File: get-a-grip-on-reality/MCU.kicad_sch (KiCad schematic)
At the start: 20 parts, among them J2 USB_OTG, U3 ESP32-S3-WROOM-1, U4 D3V3XA4B10LP, U5 TLV75801PDRV

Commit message: add new chips
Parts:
- added C10, C4, C5: 1u, symbol Device:C
- added U1: TLV76733DRVx, Package_SON:WSON-6-1EP_2x2mm_P0.65mm_EP1x1.6mm_ThermalVias, symbol Regulator_Linear:TLV76733DRVx
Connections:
- net +3.3V: now also C10.1, C5.1, U1.1 (OUT), U1.2 (SNS)
- net GND: now also C10.2, C4.2, C5.2, U1.3 (GND), U1.5 (GND), U1.7 (PAD)
- new net +BATT: C4.1, U1.4 (EN), U1.6 (IN)

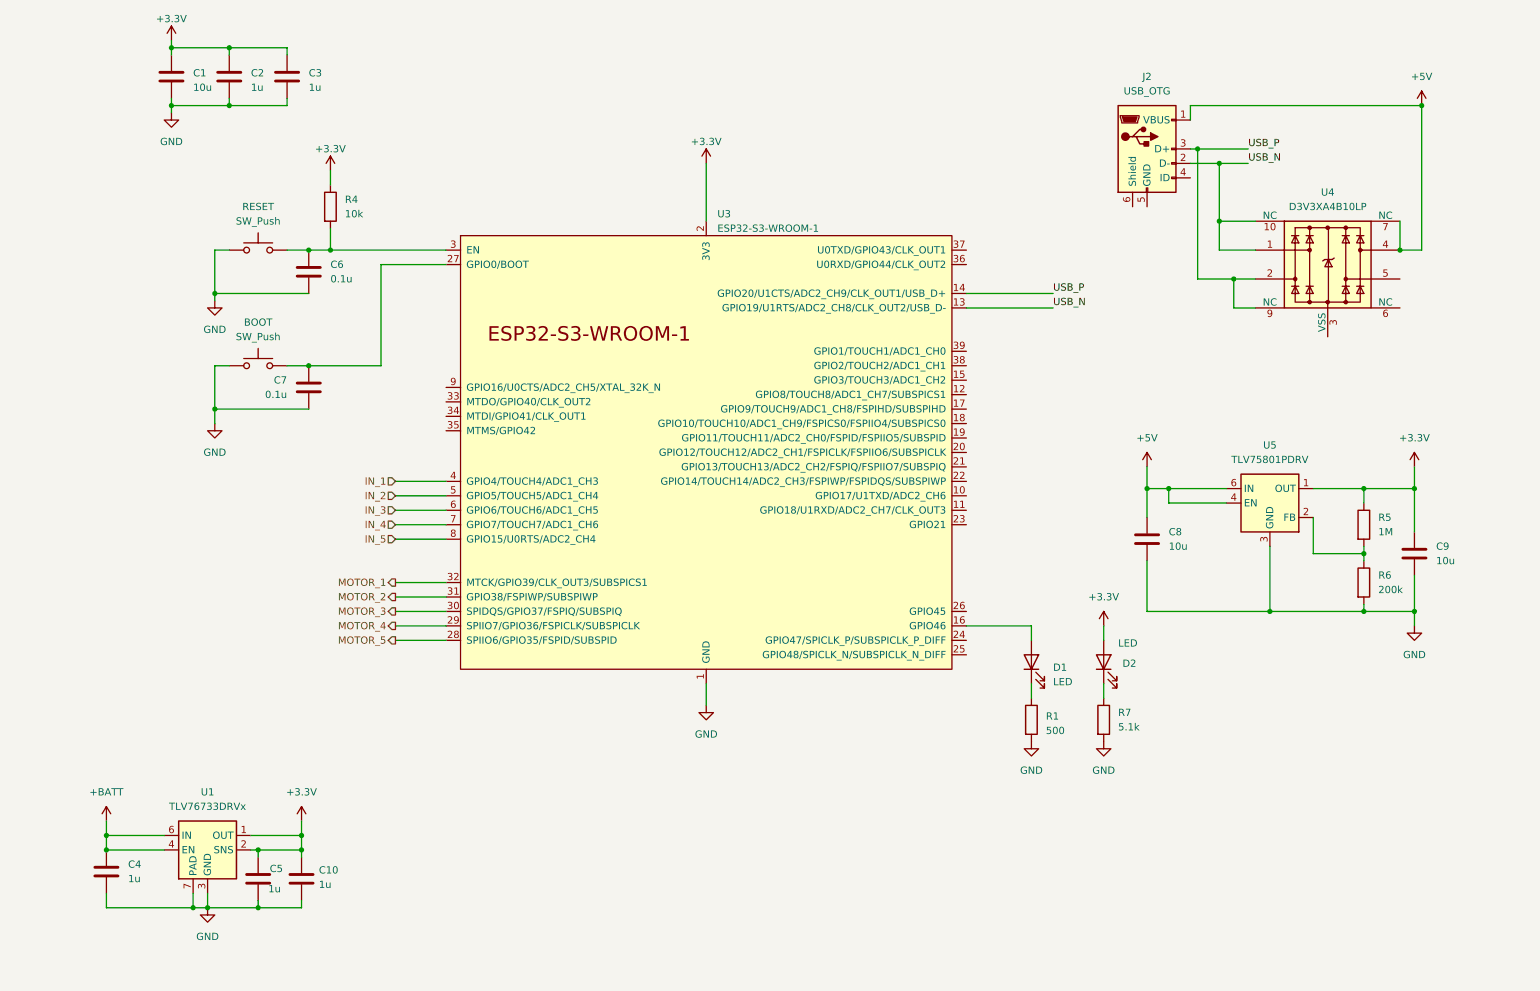
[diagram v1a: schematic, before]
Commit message: finish mcu and power page
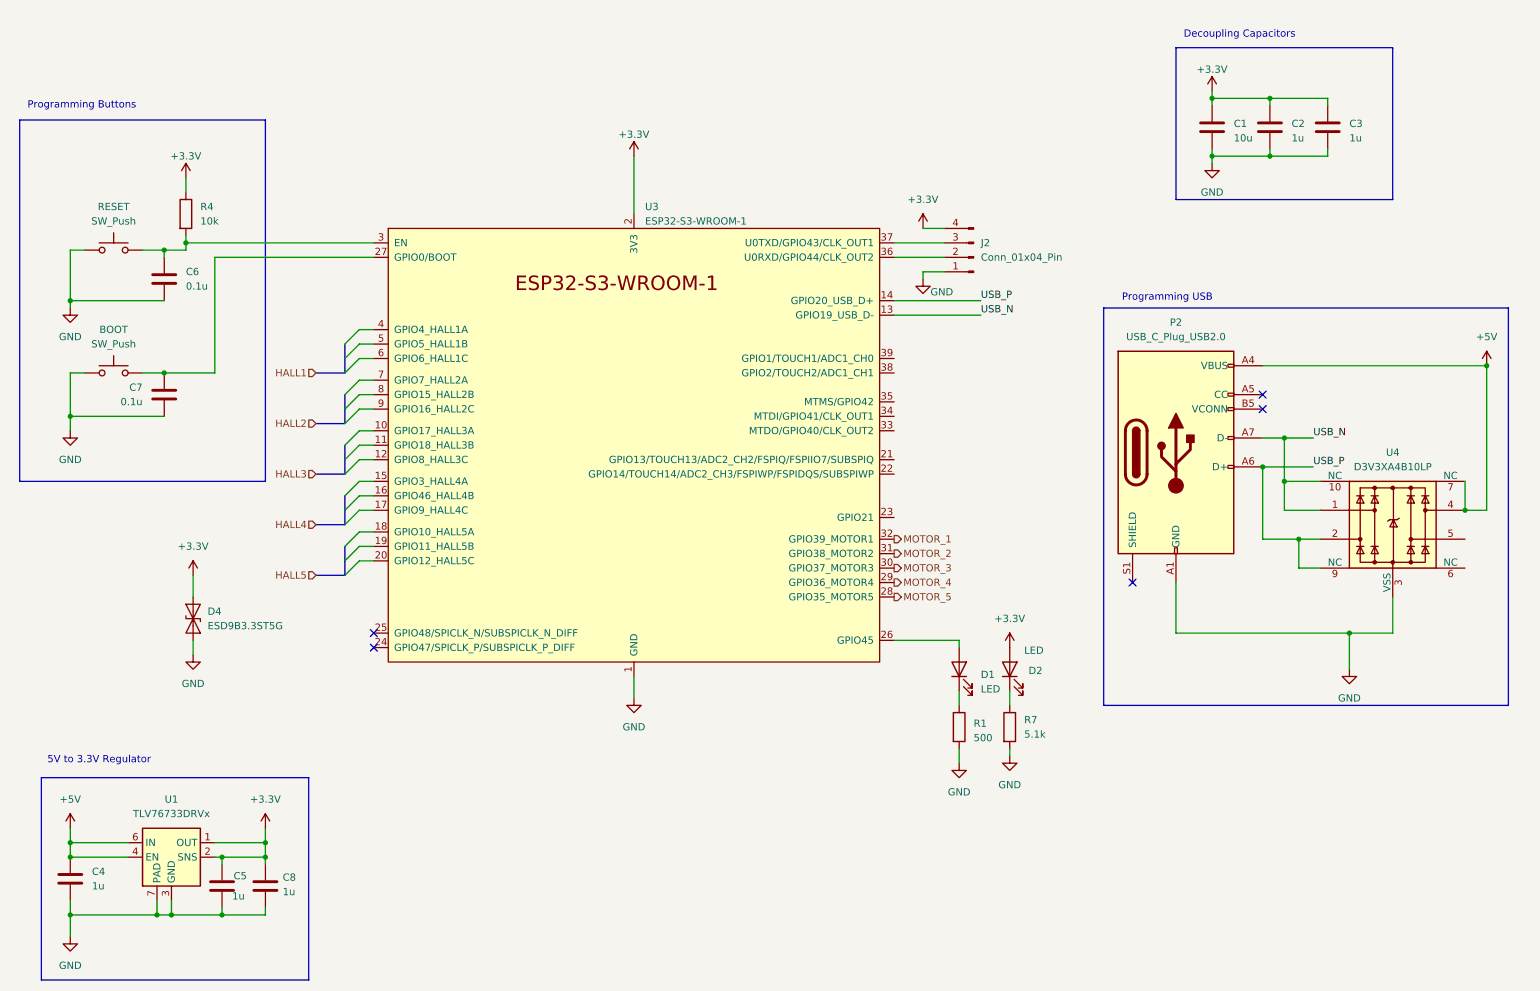
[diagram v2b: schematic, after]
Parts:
- removed C10: 1u, symbol Device:C
- removed C9: 10u, symbol Device:C
- removed J2: USB_OTG, symbol Connector:USB_OTG
- removed R5: 1M, symbol Device:R
- removed R6: 200k, symbol Device:R
- removed U5: TLV75801PDRV, Package_SON:WSON-6-1EP_2x2mm_P0.65mm_EP1x1.6mm, symbol Regulator_Linear:TLV75801PDRV
- added D4: ESD9B3.3ST5G, Diode_SMD:D_SOD-923, symbol Diode:ESD9B3.3ST5G
- added J2: Conn_01x04_Pin, Connector_PinHeader_2.54mm:PinHeader_1x04_P2.54mm_Vertical, symbol Connector:Conn_01x04_Pin
- added P2: USB_C_Plug_USB2.0, symbol Connector:USB_C_Plug_USB2.0
- C8: value 10u -> 1u
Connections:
- net +BATT is gone; now on net +5V: C4.1, U1.4 (EN), U1.6 (IN)
- net +3.3V: now also C8.1, D4.2 (A2), J2.4 (Pin_4)
- net +5V: now also P2.A4 (VBUS), P2.A9 (VBUS), P2.B4 (VBUS), P2.B9 (VBUS); no longer C8.1
- net GND: now also U4.3 (VSS), U4.8 (VSS), D4.1 (A1), J2.1 (Pin_1), P2.A1 (GND), P2.A12 (GND), P2.B1 (GND), P2.B12 (GND)
- net USB_N: now also P2.A7 (D-)
- net USB_P: now also P2.A6 (D+)
- net at D1.2 (A): now also U3.26 (GPIO45); no longer U3.16 (GPIO46)
- net at U3.36 (U0RXD/GPIO44/CLK_OUT2): now also J2.2 (Pin_2)
- net at U3.37 (U0TXD/GPIO43/CLK_OUT1): now also J2.3 (Pin_3)
- net IN_1: no longer names the net of U3.4 (GPIO4_HALL1A)
- net IN_2: no longer names the net of U3.5 (GPIO5_HALL1B)
- net IN_3: no longer names the net of U3.6 (GPIO6_HALL1C)
- net IN_4: no longer names the net of U3.7 (GPIO7_HALL2A)
- net IN_5: no longer names the net of U3.8 (GPIO15_HALL2B)
- no-connect marks 0 -> 5
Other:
- note added: "5V to 3.3V Regulator"
- note added: "Decoupling Capacitors"
- note added: "Programming Buttons"
- note added: "Programming USB"
- moved on the sheet: BOOT, C1, C2, C3, C6, C7, D1, D2, R1, R4, R7, RESET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

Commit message: add output
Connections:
- net +5V: no longer P2.A4 (VBUS), P2.A9 (VBUS), P2.B4 (VBUS), P2.B9 (VBUS), U4.4, U4.7 (NC)
- net at D1.2 (A): now also U3.23 (GPIO21); no longer U3.26 (GPIO45)
- net HALL3A: now reaches U3.10 (GPIO17_HALL3A)
- net HALL3B: now reaches U3.11 (GPIO18_HALL3B)
- net HALL3C: now reaches U3.12 (GPIO8_HALL3C)
- net HALL4A: now reaches U3.15 (GPIO3_HALL4A)
- net HALL4B: now reaches U3.17 (GPIO9_HALL4B)
- net HALL4C: now reaches U3.18 (GPIO10_HALL4C)
- net HALL5A: now reaches U3.19 (GPIO11_HALL5A)
- net HALL5B: now reaches U3.20 (GPIO12_HALL5B)
- net HALL5C: now reaches U3.21 (GPIO13_HALL5C)
- net SDI: now reaches U3.33 (GPIO40_MTDO)
- net SDO: now reaches U3.34 (GPIO41_MTDI)
- net SCS: now reaches U3.35 (GPIO42_MTMS)
- net INT2: now reaches U3.38 (GPIO2/TOUCH2/ADC1_CH1)
- net INT1: now reaches U3.39 (GPIO1/TOUCH1/ADC1_CH0)
- net HALL1A: now reaches U3.4 (GPIO4_HALL1A)
- net HALL1B: now reaches U3.5 (GPIO5_HALL1B)
- net HALL1C: now reaches U3.6 (GPIO6_HALL1C)
- net HALL2A: now reaches U3.7 (GPIO7_HALL2A)
- net HALL2B: now reaches U3.8 (GPIO15_HALL2B)
- net HALL2C: now reaches U3.9 (GPIO16_HALL2C)
- net MOTOR_1 renamed SCLK
- net MOTOR_2 renamed MOTOR1
- net MOTOR_3 renamed MOTOR2
- net MOTOR_4 renamed MOTOR3
- net MOTOR_5 renamed MOTOR4
- new net MOTOR5: U3.26 (GPIO45_MOTOR5)
- new net VBUS: P2.A4 (VBUS), P2.A9 (VBUS), P2.B4 (VBUS), P2.B9 (VBUS), U4.4, U4.7 (NC)
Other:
- moved on the sheet: C4, D1, D2

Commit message: add more to pcb
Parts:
- added J15: Battery Connector MCU, Connector_AMASS:AMASS_XT30PW-M_1x02_P2.50mm_Horizontal, symbol Connector:Conn_01x02_Socket
- BOOT1: renamed from BOOT; footprint (none) -> Button_Switch_SMD:SW_SPST_EVPBF
- C1: renamed from C4; footprint (none) -> Capacitor_SMD:C_0805_2012Metric
- C2: renamed from C6; footprint (none) -> Capacitor_SMD:C_0805_2012Metric
- C3: renamed from C7; footprint (none) -> Capacitor_SMD:C_0805_2012Metric
- C4: renamed from C5; footprint (none) -> Capacitor_SMD:C_0805_2012Metric
- C5: renamed from C8; footprint (none) -> Capacitor_SMD:C_0805_2012Metric
- C6: renamed from C1; footprint (none) -> Capacitor_SMD:C_0805_2012Metric
- C7: renamed from C2; footprint (none) -> Capacitor_SMD:C_0805_2012Metric
- C8: renamed from C3; footprint (none) -> Capacitor_SMD:C_0805_2012Metric
- D2: renamed from D1; footprint (none) -> LED_SMD:LED_0805_2012Metric
- D3: renamed from D2; footprint (none) -> LED_SMD:LED_0805_2012Metric
- P1: renamed from P2; footprint (none) -> Connector_USB:USB_C_Receptacle_GCT_USB4110
- R1: renamed from R4; footprint (none) -> Resistor_SMD:R_0805_2012Metric
- R2: renamed from R1; footprint (none) -> Resistor_SMD:R_0805_2012Metric
- R3: renamed from R7; footprint (none) -> Resistor_SMD:R_0805_2012Metric
- RESET1: renamed from RESET; footprint (none) -> Button_Switch_SMD:SW_SPST_EVPBF
- U2: renamed from U3; footprint esp32-s3-wroom-1:ESP32-S3-WROOM-1-N8_EXP -> RF_Module:ESP32-S3-WROOM-1
- renumbered D4 to D1, J2 to J12, U4 to U3
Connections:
- net +3.3V: now also J12.1 (Pin_1); no longer J12.4 (Pin_4)
- net +5V: now also J15.1 (Pin_1)
- net GND: now also J12.4 (Pin_4), J15.2 (Pin_2); no longer J12.1 (Pin_1)
- net at J12.2 (Pin_2): now also U2.37 (U0TXD/GPIO43/CLK_OUT1); no longer U2.36 (U0RXD/GPIO44/CLK_OUT2)
- net at J12.3 (Pin_3): now also U2.36 (U0RXD/GPIO44/CLK_OUT2); no longer U2.37 (U0TXD/GPIO43/CLK_OUT1)
- no-connect marks 5 -> 8
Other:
- moved on the sheet: C4, C5, J12

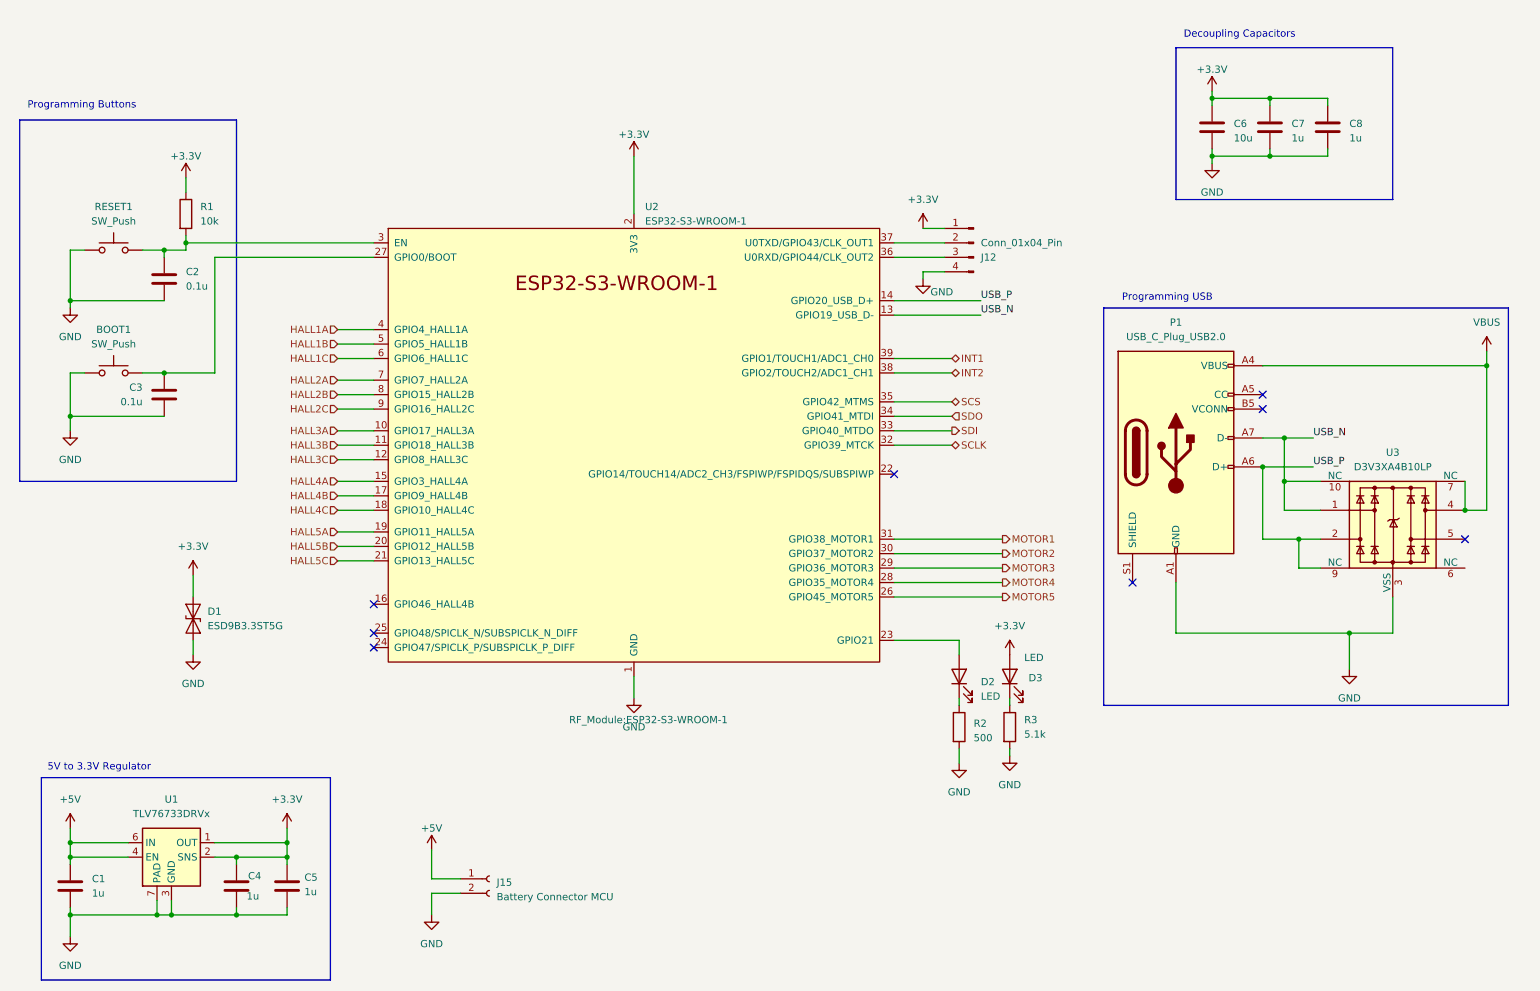
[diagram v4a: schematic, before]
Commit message: fix schematic with winstons suggestions
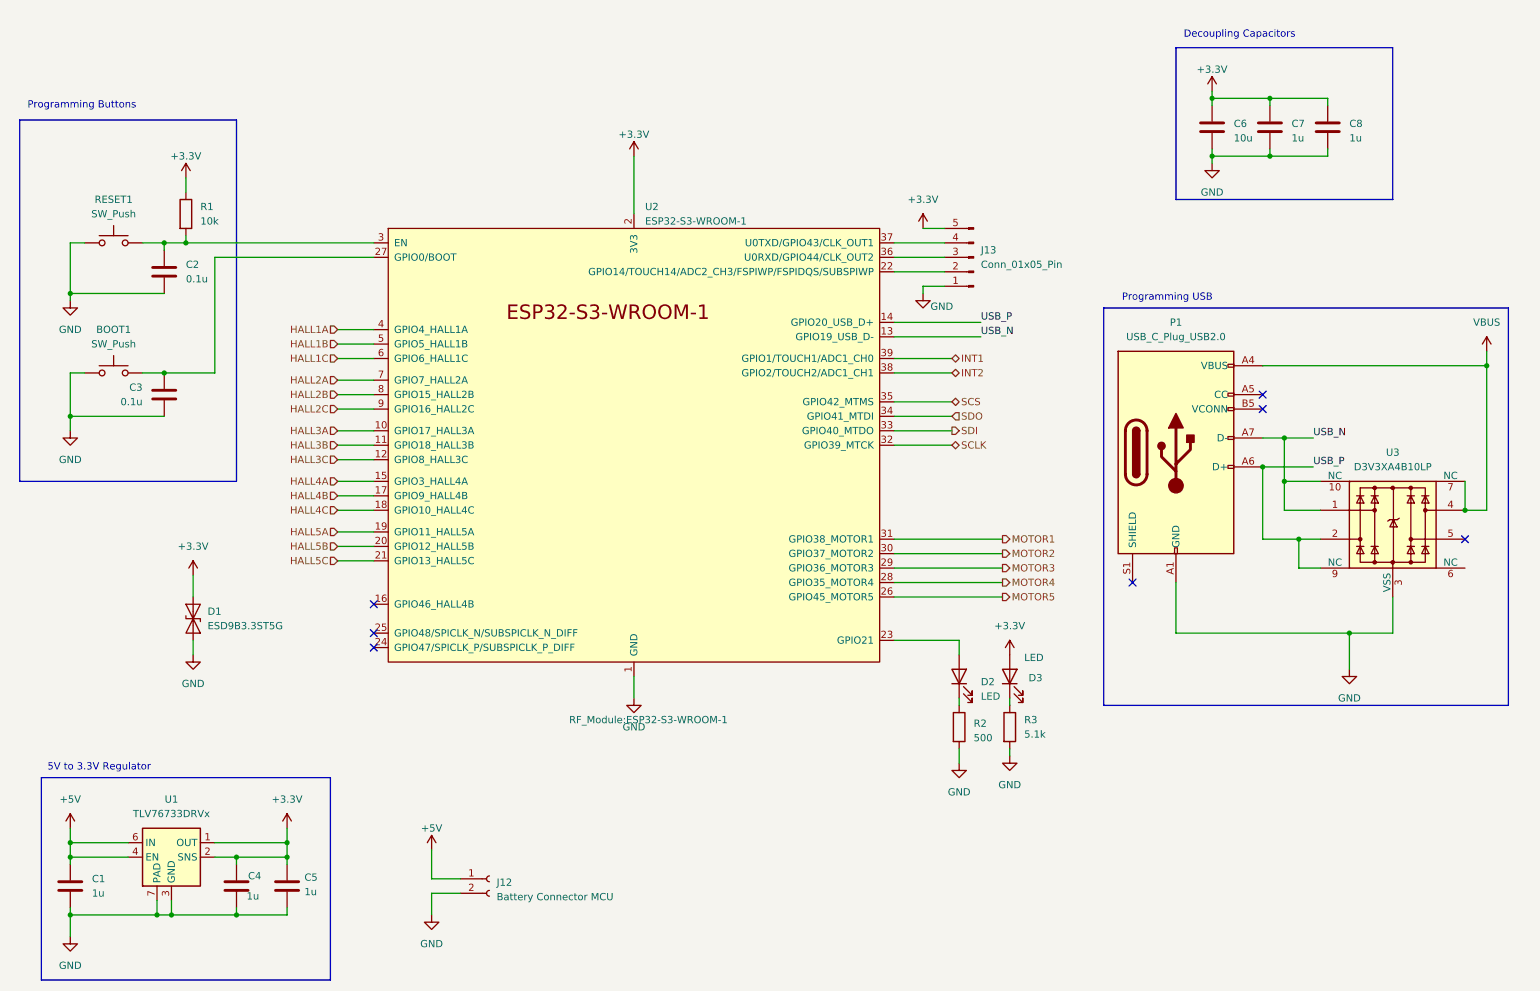
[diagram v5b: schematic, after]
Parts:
- removed J12: Conn_01x04_Pin, Connector_PinHeader_2.54mm:PinHeader_1x04_P2.54mm_Vertical, symbol Connector:Conn_01x04_Pin
- added J13: Conn_01x05_Pin, symbol Connector:Conn_01x05_Pin
- renumbered J15 to J12
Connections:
- net +3.3V: now also J13.5 (Pin_5)
- net GND: now also J13.1 (Pin_1)
- net at U2.37 (U0TXD/GPIO43/CLK_OUT1): now also J13.4 (Pin_4)
- net at U2.36 (U0RXD/GPIO44/CLK_OUT2): now also J13.3 (Pin_3)
- net at U2.22 (GPIO14/TOUCH14/ADC2_CH3/FSPIWP/FSPIDQS/SUBSPIWP): now also J13.2 (Pin_2)
- no-connect marks 8 -> 7
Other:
- moved on the sheet: C2, RESET1

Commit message: finish top pcb
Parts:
- J13: footprint (none) -> Connector_PinHeader_2.54mm:PinHeader_1x05_P2.54mm_Vertical
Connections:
- net VBUS is gone; now on net +5V: P1.A4 (VBUS), P1.A9 (VBUS), P1.B4 (VBUS), P1.B9 (VBUS), U3.4, U3.7 (NC)
- net +3.3V: now also J13.1 (Pin_1); no longer J13.5 (Pin_5)
- net GND: now also J13.5 (Pin_5); no longer J13.1 (Pin_1)
- net at J13.2 (Pin_2): now also U2.37 (U0TXD/GPIO43/CLK_OUT1); no longer U2.22 (GPIO14/TOUCH14/ADC2_CH3/FSPIWP/FSPIDQS/SUBSPIWP)
- net at J13.4 (Pin_4): now also U2.16 (GPIO46); no longer U2.37 (U0TXD/GPIO43/CLK_OUT1)
- new net LIGHT_IN: U2.22 (GPIO14_LIGHT_IN)
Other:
- moved on the sheet: J13
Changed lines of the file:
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@@
 	(wire
 		(pts
+			(xy 175.26 128.27) (xy 180.34 128.27)
+		)
+		(stroke
+			(width 0)
+			(type default)
+		)
+	)
+	(wire
+		(pts
 			(xy 68.58 170.18) (xy 68.58 168.91)
 		)
@@
 		)
 	)
+	(hierarchical_label "LIGHT_IN"
+		(shape input)
+		(at 180.34 128.27 0)
+		(fields_autoplaced yes)
+		(effects
+			(font
+				(size 1.27 1.27)
+			)
+			(justify left)
+		)
+	)
 	(hierarchical_label "HALL2B"
 		(shape input)
@@
 	(symbol
 		(lib_id "Connector:Conn_01x05_Pin")
-		(at 189.23 63.5 180)
+		(at 189.23 63.5 0)
+		(mirror y)
 		(unit 1)
 		(exclude_from_sim no)
@@
 		(on_board yes)
 		(dnp no)
-		(fields_autoplaced yes)
 		(property "Reference" "J13"
-			(at 190.5 62.2299 0)
+			(at 190.5 64.7701 0)
 			(effects
 				(font
@@
 		)
 		(property "Value" "Conn_01x05_Pin"
-			(at 190.5 64.7699 0)
+			(at 190.5 62.2301 0)
 			(effects
 				(font
@@
 			)
 		)
-		(property "Footprint" ""
+		(property "Footprint" "Connector_PinHeader_2.54mm:PinHeader_1x05_P2.54mm_Vertical"
 			(at 189.23 63.5 0)
 			(effects
@@
 	)
 	(symbol
+		(lib_id "power:+5V")
+		(at 279.4 80.01 0)
+		(unit 1)
+		(exclude_from_sim no)
+		(in_bom yes)
+		(on_board yes)
+		(dnp no)
+		(property "Reference" "#PWR043"
+			(at 279.4 83.82 0)
+			(effects
+				(font
+					(size 1.27 1.27)
+				)
+				(hide yes)
+			)
+		)
+		(property "Value" "+5V"
+			(at 279.4 74.93 0)
+			(effects
+				(font
+					(size 1.27 1.27)
+				)
+			)
+		)
+		(property "Footprint" ""
+			(at 279.4 80.01 0)
+			(effects
+				(font
+					(size 1.27 1.27)
+				)
+				(hide yes)
+			)
+		)
+		(property "Datasheet" ""
+			(at 279.4 80.01 0)
+			(effects
+				(font
+					(size 1.27 1.27)
+				)
+				(hide yes)
+			)
+		)
+		(property "Description" "Power symbol creates a global label with name \"+5V\""
+			(at 279.4 80.01 0)
+			(effects
+				(font
+					(size 1.27 1.27)
+				)
+				(hide yes)
+			)
+		)
+		(pin "1"
+		)
+		(instances
+			(project "get-a-grip-on-reality"
+				(path "/baa0c64e-005f-4609-8fc2-3159870af962/ac4bf6b8-92c6-4d58-8d59-9dba1bb4caf0"
+					(reference "#PWR043")
+					(unit 1)
+				)
+			)
+		)
+	)
+	(symbol
 		(lib_id "power:GND")
 		(at 186.69 152.4 0)
@@
 					(unit 1)
 				)
-			)
-		)
-	)
-	(symbol
-		(lib_id "power:+5V")
-		(at 279.4 80.01 0)
-		(unit 1)
-		(exclude_from_sim no)
-		(in_bom yes)
-		(on_board yes)
-		(dnp no)
-		(fields_autoplaced yes)
-		(property "Reference" "#PWR043"
-			(at 279.4 83.82 0)
-			(effects
-				(font
-					(size 1.27 1.27)
-				)
-				(hide yes)
-			)
-		)
-		(property "Value" "VBUS"
-			(at 279.4 74.93 0)
-			(effects
-				(font
-					(size 1.27 1.27)
-				)
-			)
-		)
-		(property "Footprint" ""
-			(at 279.4 80.01 0)
-			(effects
-				(font
-					(size 1.27 1.27)
-				)
-				(hide yes)
-			)
-		)
-		(property "Datasheet" ""
-			(at 279.4 80.01 0)
-			(effects
-				(font
-					(size 1.27 1.27)
-				)
-				(hide yes)
-			)
-		)
-		(property "Description" "Power symbol creates a global label with name \"+5V\""
-			(at 279.4 80.01 0)
-			(effects
-				(font
-					(size 1.27 1.27)
-				)
-				(hide yes)
-			)
-		)
-		(pin "1"
-		)
-		(instances
-			(project ""
-				(path "/baa0c64e-005f-4609-8fc2-3159870af962/ac4bf6b8-92c6-4d58-8d59-9dba1bb4caf0"
-					(reference "#PWR043")
-					(unit 1)
-				)
